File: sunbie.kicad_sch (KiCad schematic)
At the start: 12 parts, among them J1 Display, SW1 SW_Push_45deg, SW2 SW_Push_45deg, SW3 SW_Push_45deg, SW4 SW_Push_45deg, SW5 SW_Push_45deg, U1 XIAO-ESP32-C3-SMD, U2 MPU-6050, U3 DHT11

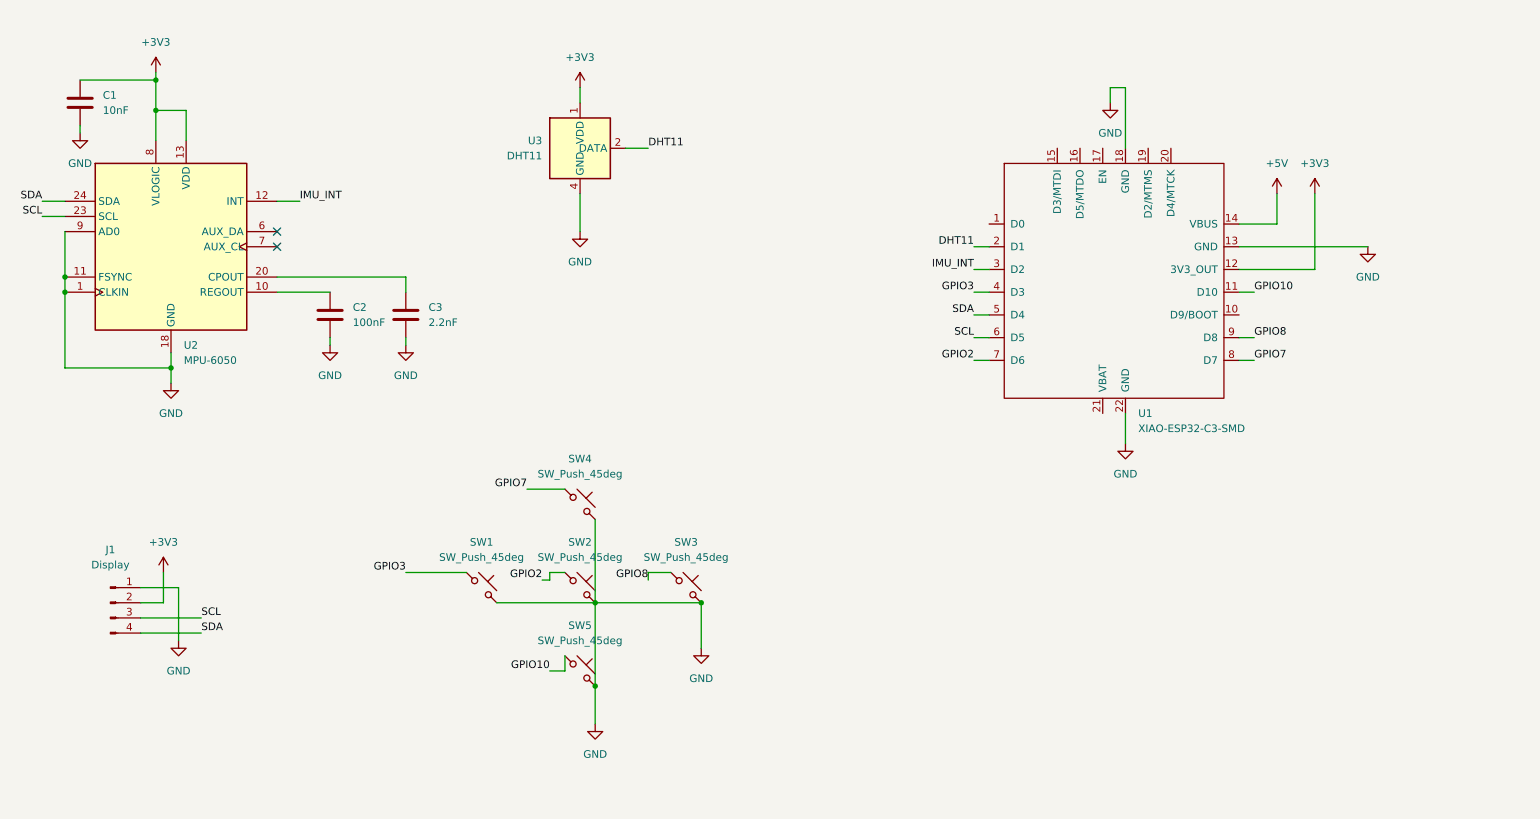
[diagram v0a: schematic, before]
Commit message: switch imu and organize schematic
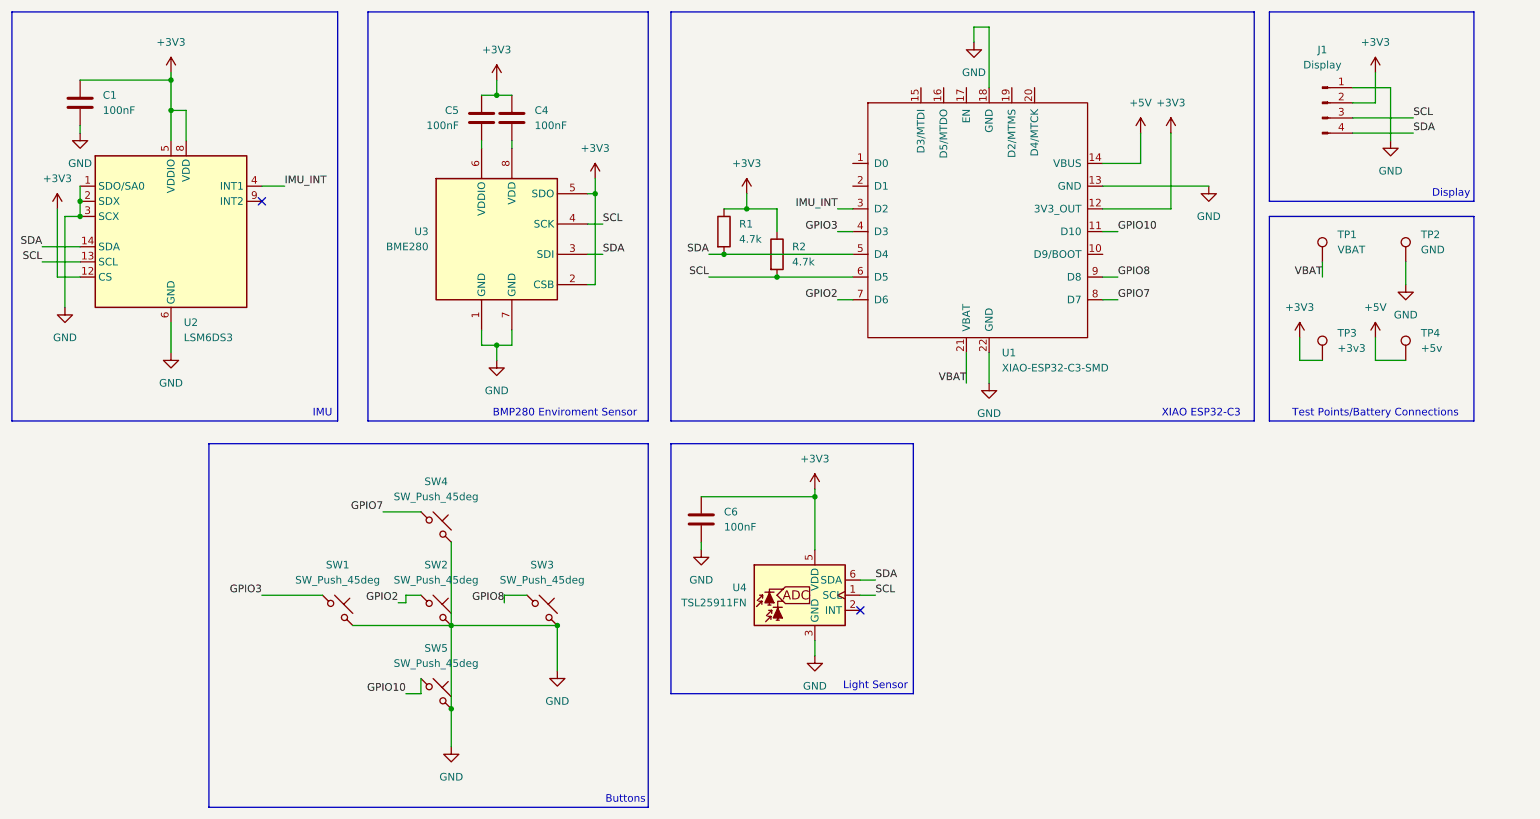
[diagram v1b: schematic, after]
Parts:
- removed C2: 100nF, Capacitor_SMD:C_0805_2012Metric_Pad1.18x1.45mm_HandSolder, symbol Device:C
- removed C3: 2.2nF, Capacitor_SMD:C_0805_2012Metric_Pad1.18x1.45mm_HandSolder, symbol Device:C
- removed U2: MPU-6050, Sensor_Motion:InvenSense_QFN-24_4x4mm_P0.5mm, symbol Sensor_Motion:MPU-6050
- removed U3: DHT11, Sensor:Aosong_DHT11_5.5x12.0_P2.54mm, symbol Sensor:DHT11
- added C4, C5, C6: 100nF, Capacitor_SMD:C_0805_2012Metric_Pad1.18x1.45mm_HandSolder, symbol Device:C
- added R1, R2: 4.7k, symbol Device:R
- added TP1: VBAT, symbol Connector:TestPoint
- added TP2: GND, symbol Connector:TestPoint
- added TP3: +3v3, symbol Connector:TestPoint
- added TP4: +5v, symbol Connector:TestPoint
- added U2: LSM6DS3, Package_LGA:LGA-14_3x2.5mm_P0.5mm_LayoutBorder3x4y, symbol Sensor_Motion:LSM6DS3
- added U3: BME280, Package_LGA:Bosch_LGA-8_2.5x2.5mm_P0.65mm_ClockwisePinNumbering, symbol Sensor:BME280
- added U4: TSL25911FN, OptoDevice:AMS_TSL25911FN, symbol Sensor_Optical:TSL25911FN
- C1: value 10nF -> 100nF
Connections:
- net +3V3: now also C4.1, C5.1, C6.1, R1.1, R2.1, TP3.1, U2.12 (CS), U2.5 (VDDIO), U2.8 (VDD), U3.2 (CSB), U3.5 (SDO), U4.5 (VDD)
- net +5V: now also TP4.1
- net GND: now also C6.2, TP2.1, U2.1 (SDO/SA0), U2.2 (SDX), U2.3 (SCX), U2.6 (GND), U2.7 (GND), U3.1 (GND), U3.7 (GND), U4.3 (GND)
- net IMU_INT: now also U2.4 (INT1)
- net SCL: now also R2.2, U2.13 (SCL), U3.4 (SCK), U4.1 (SCL)
- net SDA: now also R1.2, U2.14 (SDA), U3.3 (SDI), U4.6 (SDA)
- net VBAT: now reaches U1.21 (VBAT)
- net VBAT: now also TP1.1
- net DHT11: no longer names the net of U1.2 (D1)
- new net: C4.2, U3.8 (VDD)
- new net: C5.2, U3.6 (VDDIO)
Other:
- note added: "BMP280 Enviroment Sensor"
- note added: "Buttons"
- note added: "Display"
- note added: "IMU"
- note added: "Light Sensor"
- note added: "Test Points/Battery Connections"
- note added: "XIAO ESP32-C3"
- moved on the sheet: J1, SW1, SW2, SW3, SW4, SW5, U1

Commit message: add buzzer
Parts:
- added BZ1: Buzzer, symbol Device:Buzzer
- added Q1: BC547, Package_TO_SOT_THT:TO-92_Inline, symbol Transistor_BJT:BC547
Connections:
- net +5V: now also BZ1.1 (+)
- net GND: now also Q1.3 (E)
- net BUZZER: now reaches U1.2 (D1)
- net BUZZER: now also Q1.2 (B)
- new net: BZ1.2 (-), Q1.1 (C)
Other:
- note added: "Buzzer"

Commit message: route pcb and do layout
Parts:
- BZ1: footprint (none) -> Buzzer_Beeper:Buzzer_Murata_PKLCS1212E
- J1: footprint (none) -> footprints:Display_128x64_096_I2C
- R1, R2: footprint (none) -> Resistor_SMD:R_0805_2012Metric_Pad1.20x1.40mm_HandSolder
- SW1, SW2, SW3, SW4, SW5: footprint (none) -> Button_Switch_THT:SW_PUSH_6mm
- TP1, TP2, TP3, TP4: footprint (none) -> TestPoint:TestPoint_Pad_D4.0mm
- U1: footprint Seeed_Studio_XIAO_Series:XIAO-ESP32-C3-SMD -> Seeed Studio XIAO Series Library:XIAO-ESP32-C3-SMD
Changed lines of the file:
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@@
 	(rectangle
 		(start 181.61 86.36)
-		(end 228.6 128.27)
+		(end 217.17 128.27)
 		(stroke
 			(width 0)
@@
 	(text "Buzzer"
 		(exclude_from_sim no)
-		(at 224.79 127 0)
+		(at 213.36 127 0)
 		(effects
 			(font
@@
 			)
 		)
-		(property "Footprint" ""
+		(property "Footprint" "Button_Switch_THT:SW_PUSH_6mm"
 			(at 91.44 114.3 0)
 			(hide yes)
@@
 			)
 		)
-		(property "Footprint" ""
+		(property "Footprint" "TestPoint:TestPoint_Pad_D4.0mm"
 			(at 245.11 55.88 0)
 			(hide yes)
@@
 			)
 		)
-		(property "Footprint" "Seeed_Studio_XIAO_Series:XIAO-ESP32-C3-SMD"
+		(property "Footprint" "Seeed Studio XIAO Series Library:XIAO-ESP32-C3-SMD"
 			(at 144.272 71.374 0)
 			(hide yes)
@@
 			)
 		)
-		(property "Footprint" ""
+		(property "Footprint" "TestPoint:TestPoint_Pad_D4.0mm"
 			(at 245.11 72.39 0)
 			(hide yes)
@@
 			)
 		)
-		(property "Footprint" ""
+		(property "Footprint" "Button_Switch_THT:SW_PUSH_6mm"
 			(at 91.44 128.27 0)
 			(hide yes)
@@
 			)
 		)
-		(property "Footprint" ""
+		(property "Footprint" "Button_Switch_THT:SW_PUSH_6mm"
 			(at 74.93 114.3 0)
 			(hide yes)
@@
 			)
 		)
-		(property "Footprint" ""
+		(property "Footprint" "Button_Switch_THT:SW_PUSH_6mm"
 			(at 91.44 100.33 0)
 			(hide yes)
@@
 			)
 		)
-		(property "Footprint" ""
+		(property "Footprint" "TestPoint:TestPoint_Pad_D4.0mm"
 			(at 259.08 72.39 0)
 			(hide yes)
@@
 			)
 		)
-		(property "Footprint" ""
+		(property "Footprint" "Button_Switch_THT:SW_PUSH_6mm"
 			(at 109.22 114.3 0)
 			(hide yes)
@@
 			)
 		)
-		(property "Footprint" ""
+		(property "Footprint" "TestPoint:TestPoint_Pad_D4.0mm"
 			(at 259.08 55.88 0)
 			(hide yes)
@@
 			)
 		)
-		(property "Footprint" ""
+		(property "Footprint" "Resistor_SMD:R_0805_2012Metric_Pad1.20x1.40mm_HandSolder"
 			(at 137.922 50.8 90)
 			(hide yes)
@@
 			)
 		)
-		(property "Footprint" ""
+		(property "Footprint" "Resistor_SMD:R_0805_2012Metric_Pad1.20x1.40mm_HandSolder"
 			(at 146.812 54.61 90)
 			(hide yes)
@@
 			)
 		)
-		(property "Footprint" ""
+		(property "Footprint" "footprints:Display_128x64_096_I2C"
 			(at 240.03 29.21 0)
 			(hide yes)
@@
 			)
 		)
-		(property "Footprint" ""
+		(property "Footprint" "Buzzer_Beeper:Buzzer_Murata_PKLCS1212E"
 			(at 203.835 99.06 90)
 			(hide yes)

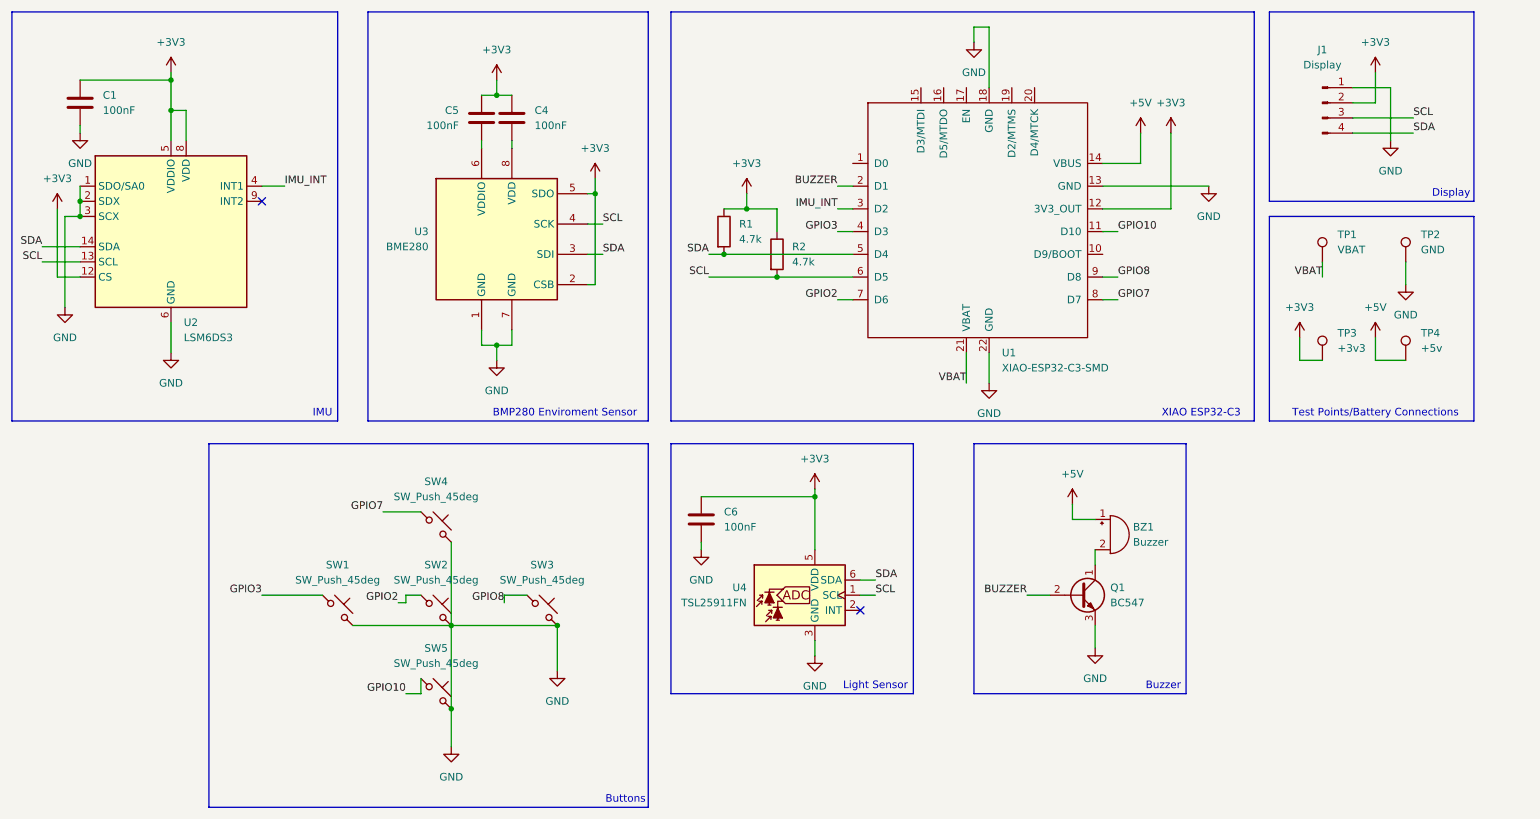
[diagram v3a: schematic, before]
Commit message: added 2 ws2812 leds
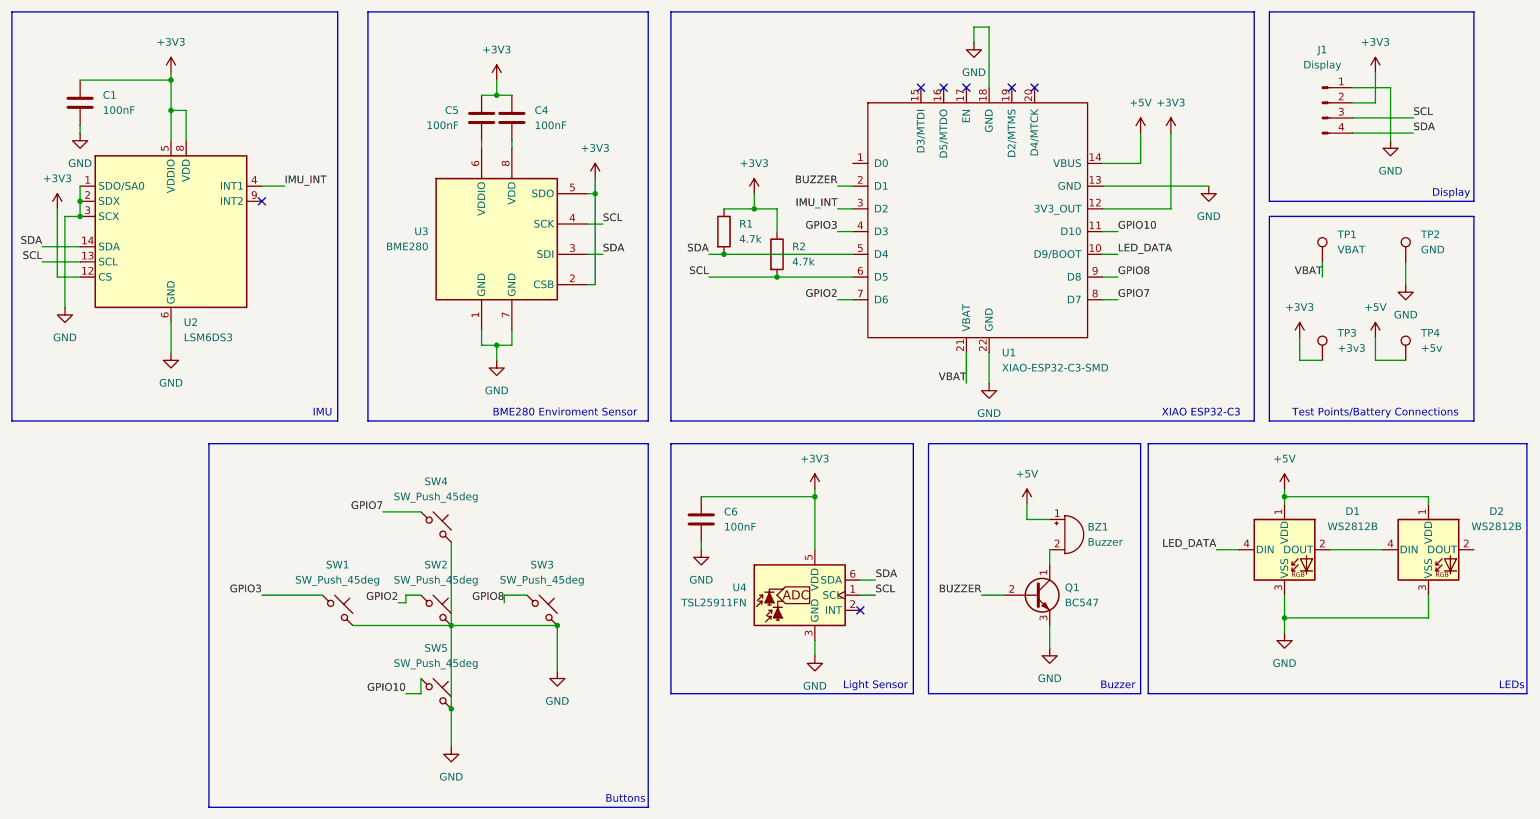
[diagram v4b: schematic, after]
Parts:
- added D1, D2: WS2812B, LED_SMD:LED_WS2812B_PLCC4_5.0x5.0mm_P3.2mm, symbol LED:WS2812B
- TP1, TP2, TP3, TP4: now left out of the parts list
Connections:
- net +5V: now also D1.1 (VDD), D2.1 (VDD)
- net GND: now also D1.3 (VSS), D2.3 (VSS)
- net LED_DATA: now reaches U1.10 (D9/BOOT)
- net LED_DATA: now also D1.4 (DIN)
- new net: D1.2 (DOUT), D2.4 (DIN)
- no-connect marks 2 -> 7
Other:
- note added: "BME280 Enviroment Sensor"
- note added: "LEDs"
- note removed: "BMP280 Enviroment Sensor"
- title: (none) -> Sunbie
- moved on the sheet: BZ1, Q1
